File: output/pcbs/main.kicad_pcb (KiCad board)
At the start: 2 copper layers, 125.8 x 86.6 mm, 22 parts

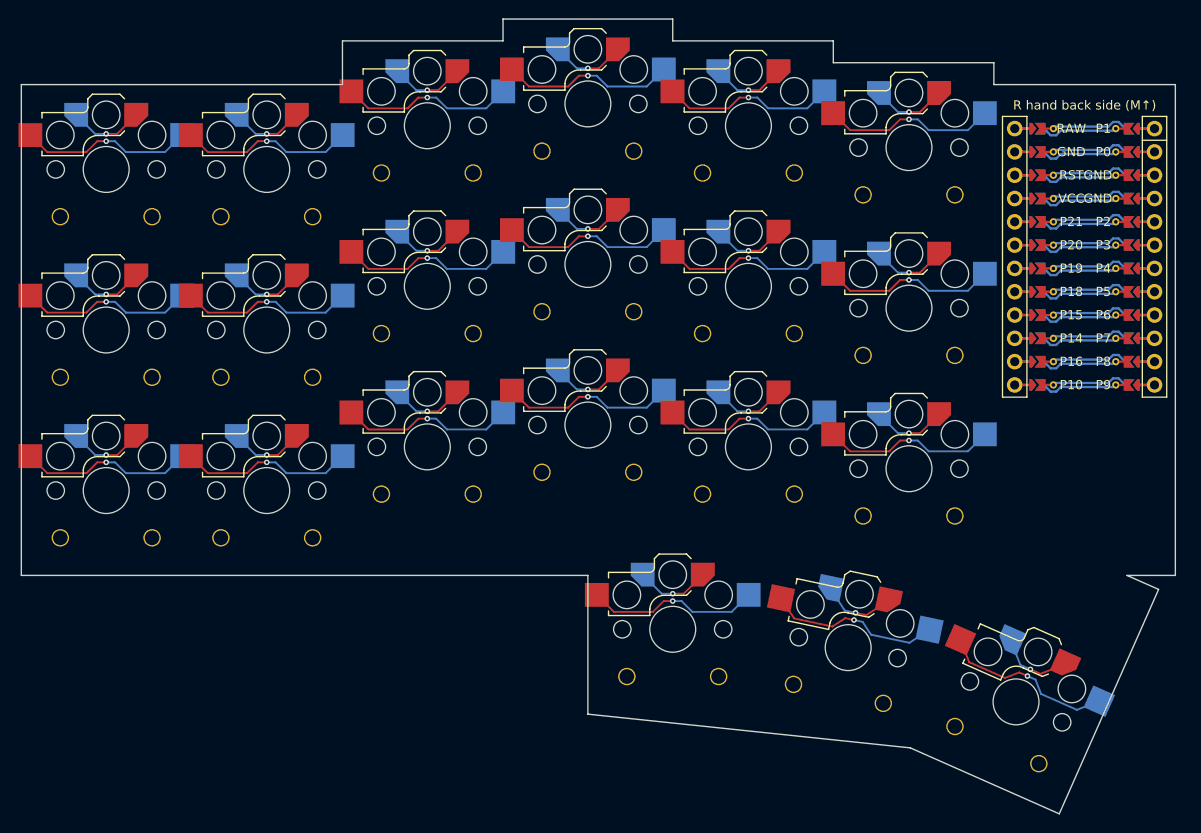
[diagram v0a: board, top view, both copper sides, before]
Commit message: feat!: update config
feat: add ref_pos outline

feat: update mcu plate calculations

feat: update thumbs plate calculations
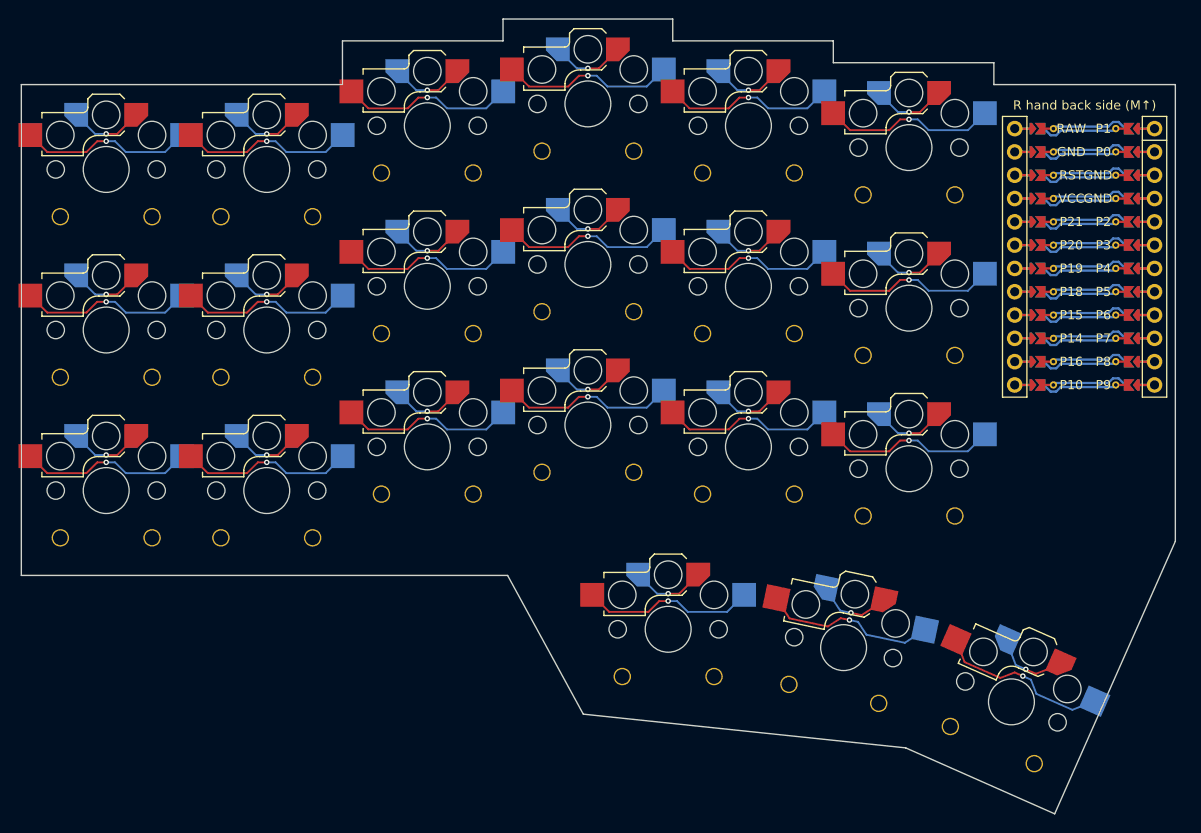
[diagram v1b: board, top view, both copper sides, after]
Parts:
- moved S19 0.50 mm to (61.2, 15.1)
- moved S20 0.50 mm to (80.4, 17.1)
- moved S21 0.50 mm to (98.7, 23.0)
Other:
- outline, holes or cut-outs redrawn
